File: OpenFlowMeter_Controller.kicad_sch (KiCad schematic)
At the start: 41 parts, among them J3 Conn_01x06, J5 Conn_01x03, J6 Conn_02x04_Odd_Even, J7 Conn_02x03_Odd_Even, U2 STM32F103C8Tx, U5 SN65HVD231, U7 24LC64, Y1 12 MHz

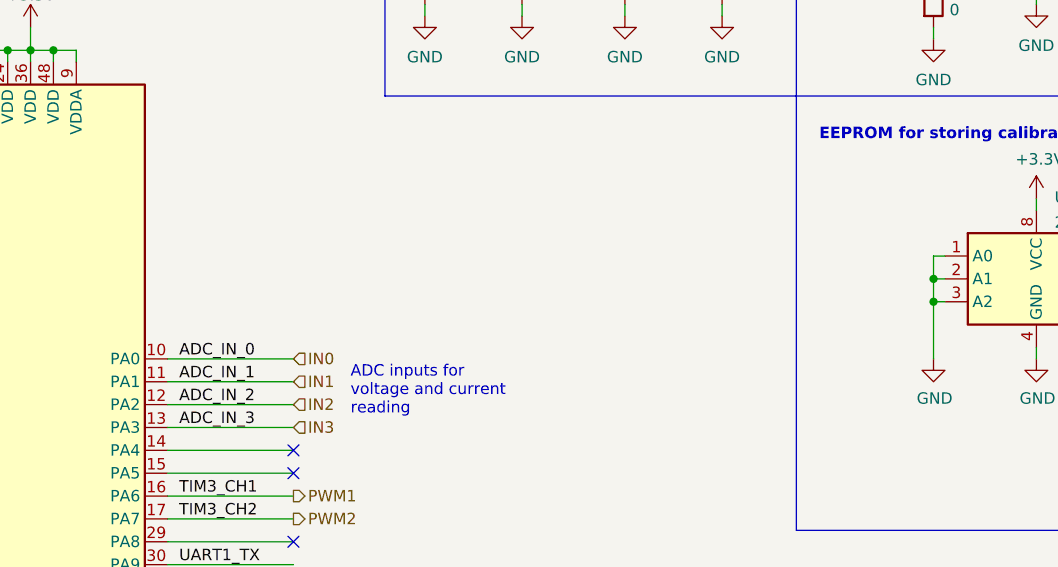
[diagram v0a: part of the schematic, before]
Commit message: include calculated results of the external impedance
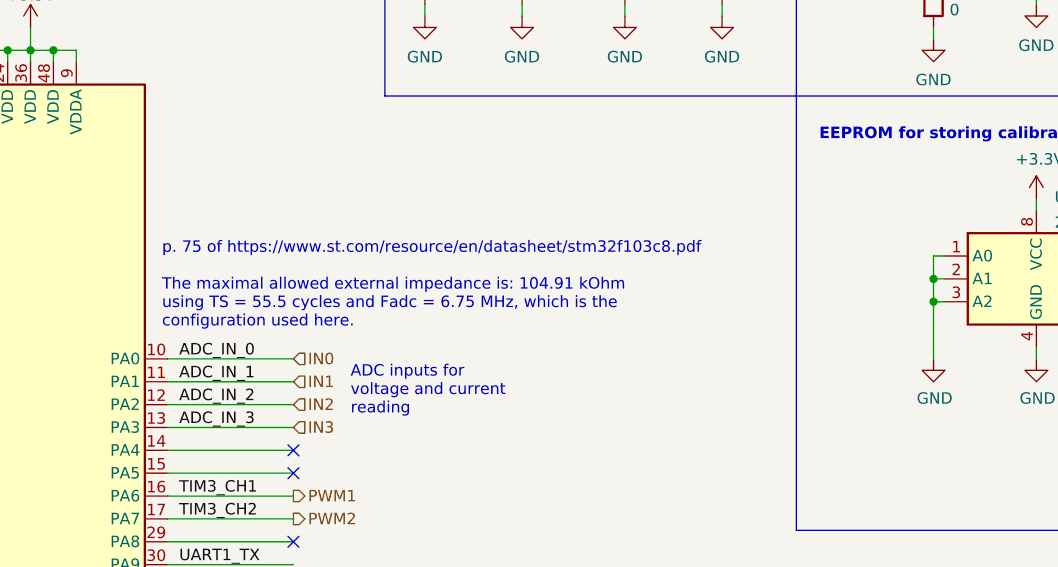
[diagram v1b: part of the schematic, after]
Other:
- note added: "p. 75 of https://www.st.com/resource/en/datasheet/stm32f103c8.pdf The maximal allowed external impedance is: 104.91 kOhm using TS = 55.5 cycles and Fadc = 6.75 MHz, which is the configuration used here."
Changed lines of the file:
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@@
     (effects (font (size 1.27 1.27) (thickness 0.254) bold) (justify left bottom))
+  )
+  (text "p. 75 of https://www.st.com/resource/en/datasheet/stm32f103c8.pdf\n\nThe maximal allowed external impedance is: 104.91 kOhm\nusing TS = 55.5 cycles and Fadc = 6.75 MHz, which is the \nconfiguration used here.\n  "
+    (at 135.255 82.55 0)
+    (effects (font (size 1.27 1.27)) (justify left bottom))
   )
   (text "I2C address: 0x50" (at 238.76 66.04 0)

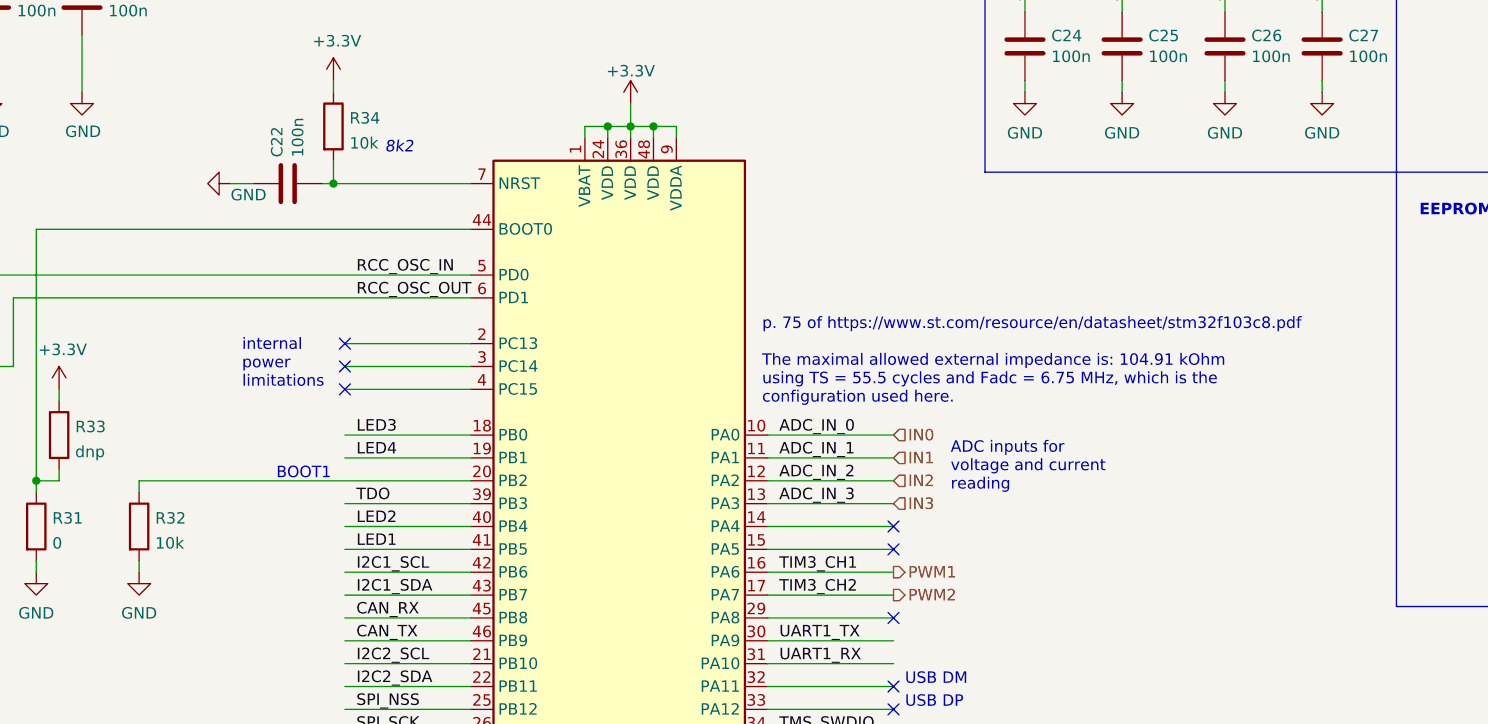
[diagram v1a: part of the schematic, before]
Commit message: inlcuded switching gain amplifier
aim is to increase the voltage and current reading for small currents and voltages.
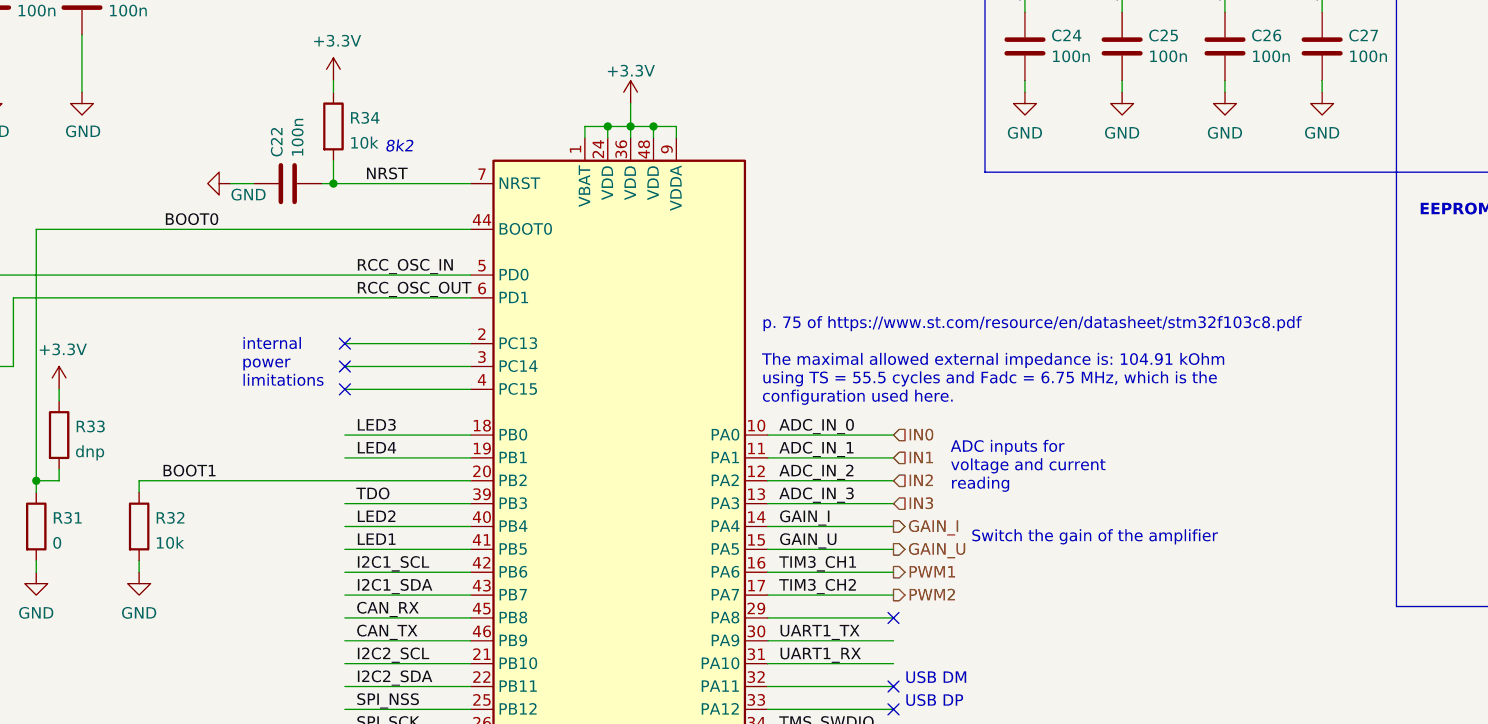
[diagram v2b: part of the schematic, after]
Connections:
- net BOOT1: now reaches R32.1, U2.20 (PB2)
- net BOOT0: now reaches R31.1, R33.2, U2.44 (BOOT0)
- net NRST: now reaches C22.2, R34.2, U2.7 (NRST)
- net GAIN_I: now reaches U2.14 (PA4)
- net GAIN_U: now reaches U2.15 (PA5)
- no-connect marks 9 -> 7
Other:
- note added: "Switch the gain of the amplifier"
- note removed: "BOOT1"
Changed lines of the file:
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@@
   (no_connect (at 149.86 104.14))
   (no_connect (at 149.86 111.76))
-  (no_connect (at 149.86 93.98))
-  (no_connect (at 149.86 96.52))
   (no_connect (at 149.86 114.3))
   (no_connect (at 88.9 73.66))
@@
     (effects (font (size 1.27 1.27) italic) (justify left bottom))
   )
+  (text "Switch the gain of the amplifier" (at 158.496 96.012 0)
+    (effects (font (size 1.27 1.27)) (justify left bottom))
+  )
   (text "JTAG 4 pin debug interface" (at 156.21 118.11 0)
     (effects (font (size 1.27 1.27)) (justify left bottom))
@@
     (effects (font (size 1.27 1.27)) (justify left bottom))
   )
-  (text "BOOT1" (at 81.28 88.9 0)
-    (effects (font (size 1.27 1.27)) (justify left bottom))
-  )
   (label "RCC_OSC_OUT" (at 90.17 68.58 0)
     (effects (font (size 1.27 1.27)) (justify left bottom))
@@
     (effects (font (size 1.27 1.27)) (justify left bottom))
   )
+  (label "NRST" (at 91.186 55.88 0)
+    (effects (font (size 1.27 1.27)) (justify left bottom))
+  )
   (label "TMS_SWDIO" (at 137.16 116.84 0)
     (effects (font (size 1.27 1.27)) (justify left bottom))
@@
     (effects (font (size 1.27 1.27)) (justify left bottom))
   )
+  (label "GAIN_I" (at 137.16 93.98 0)
+    (effects (font (size 1.27 1.27)) (justify left bottom))
+  )
   (label "CAN_RX" (at 90.17 104.14 0)
     (effects (font (size 1.27 1.27)) (justify left bottom))
@@
     (effects (font (size 1.27 1.27)) (justify left bottom))
   )
+  (label "GAIN_U" (at 137.16 96.52 0)
+    (effects (font (size 1.27 1.27)) (justify left bottom))
+  )
   (label "LED1" (at 109.22 190.5 90)
     (effects (font (size 1.27 1.27)) (justify left bottom))
@@
     (effects (font (size 1.27 1.27)) (justify left bottom))
   )
+  (label "BOOT0" (at 68.834 60.96 0)
+    (effects (font (size 1.27 1.27)) (justify left bottom))
+  )
   (label "I2C1_SCL" (at 44.45 180.34 0)
     (effects (font (size 1.27 1.27)) (justify left bottom))
@@
     (effects (font (size 1.27 1.27)) (justify left bottom))
   )
+  (label "BOOT1" (at 68.58 88.9 0)
+    (effects (font (size 1.27 1.27)) (justify left bottom))
+  )
   (label "ADC_IN_0" (at 137.16 83.82 0)
     (effects (font (size 1.27 1.27)) (justify left bottom))
@@
   (label "TIM3_CH2" (at 137.16 101.6 0)
     (effects (font (size 1.27 1.27)) (justify left bottom))
+  )
+  (hierarchical_label "GAIN_U" (shape output) (at 149.86 96.52 0)
+    (effects (font (size 1.27 1.27)) (justify left))
   )
   (hierarchical_label "IN2" (shape input) (at 149.86 88.9 0)
@@
     (effects (font (size 1.27 1.27)) (justify left))
   )
+  (hierarchical_label "GAIN_I" (shape output) (at 149.86 93.98 0)
+    (effects (font (size 1.27 1.27)) (justify left))
+  )

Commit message: added company to all schematic pages
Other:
- company: (none) -> Jochen Steinmann
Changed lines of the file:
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@@
     (title "Open Flow Meter")
     (date "2021-03-30")
-    (rev "1")
+    (rev "2")
+    (company "Jochen Steinmann")
   )
   (junction (at 38.1 76.2) (diameter 0) (color 0 0 0 0)
